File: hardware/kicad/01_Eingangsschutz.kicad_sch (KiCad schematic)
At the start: 4 parts, among them K101 G6S-2F DC5 - C16707, Q111 DMN2056U-7

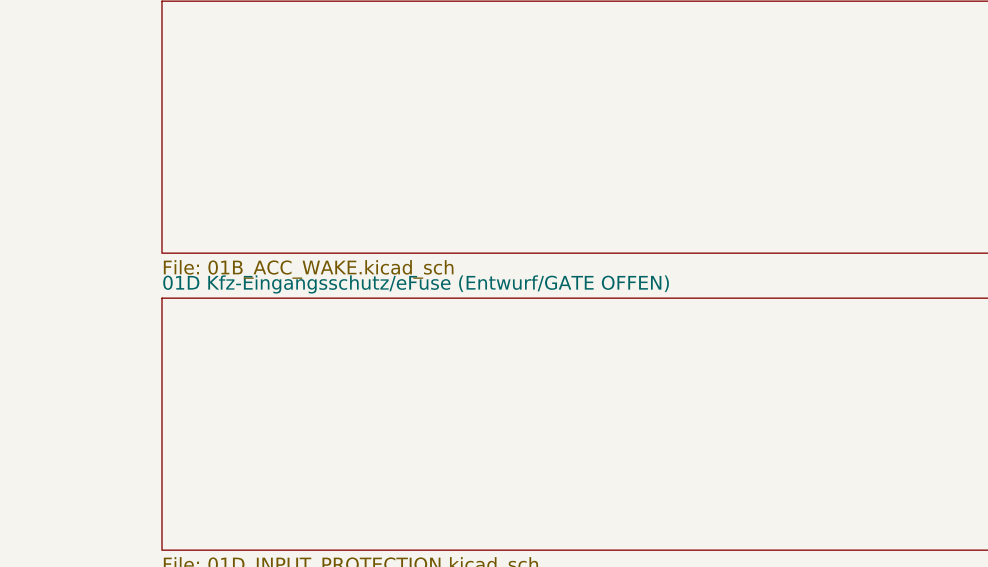
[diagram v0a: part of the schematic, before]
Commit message: hardware(kicad): mark obsolete TPS26631 sheet as retired in hierarchy
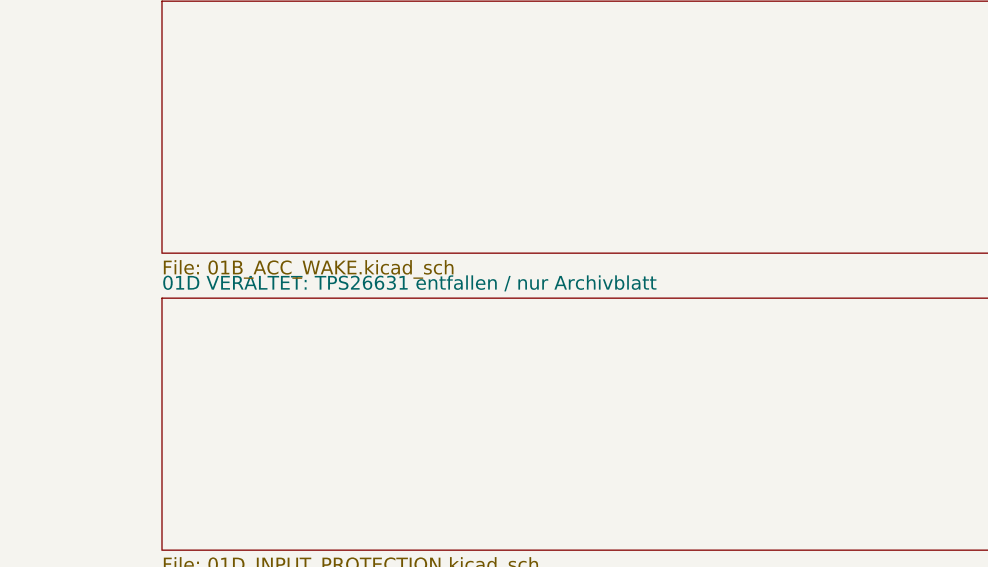
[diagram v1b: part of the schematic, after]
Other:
- sheet 01D Kfz-Eingangsschutz/eFuse (Entwurf/GATE OFFEN) renamed 01D VERALTET: TPS26631 entfallen / nur Archivblatt
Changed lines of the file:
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@@
 (sheet (at 214 290) (size 175 28) (exclude_from_sim no) (in_bom yes) (on_board yes) (dnp no)
  (stroke (width 0) (type solid)) (fill (color 0 0 0 0))
- (property "Sheetname" "01D Kfz-Eingangsschutz/eFuse (Entwurf/GATE OFFEN)" (at 214 289.24 0) (effects (font (size 1.524 1.524)) (justify left bottom)))
+ (property "Sheetname" "01D VERALTET: TPS26631 entfallen / nur Archivblatt" (at 214 289.24 0) (effects (font (size 1.524 1.524)) (justify left bottom)))
  (property "Sheetfile" "01D_INPUT_PROTECTION.kicad_sch" (at 214 318.76 0) (effects (font (size 1.524 1.524)) (justify left top)))
  (instances (project "TripTracer_V1" (path "/a26d9b0c-7f10-4e5a-a65f-000000000064/a26d9b0c-7f10-4e5a-a65f-000000000065" (page "2.4"))))

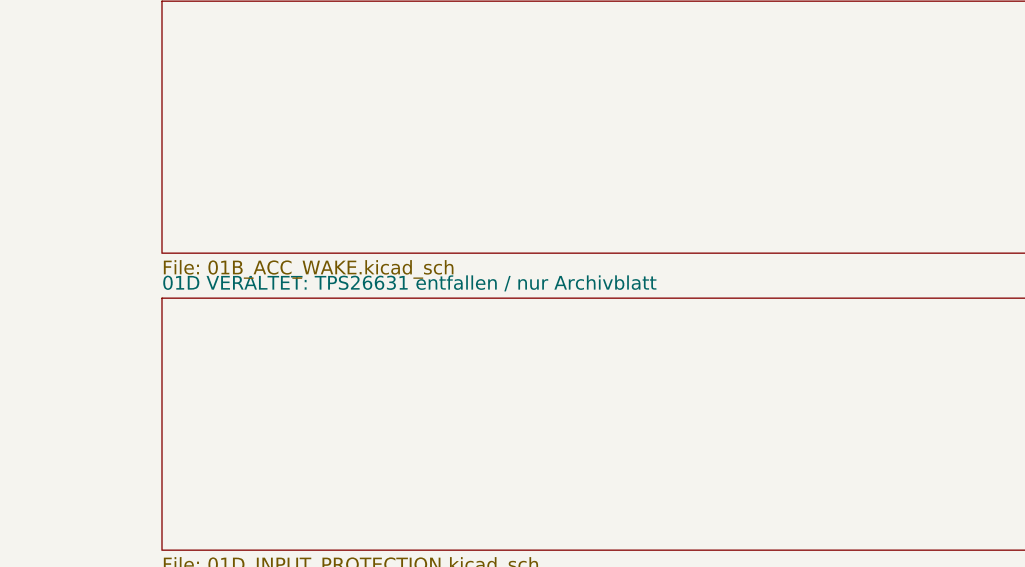
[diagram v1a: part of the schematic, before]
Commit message: hardware(kicad): identify active LM74930 core sheet in hierarchy
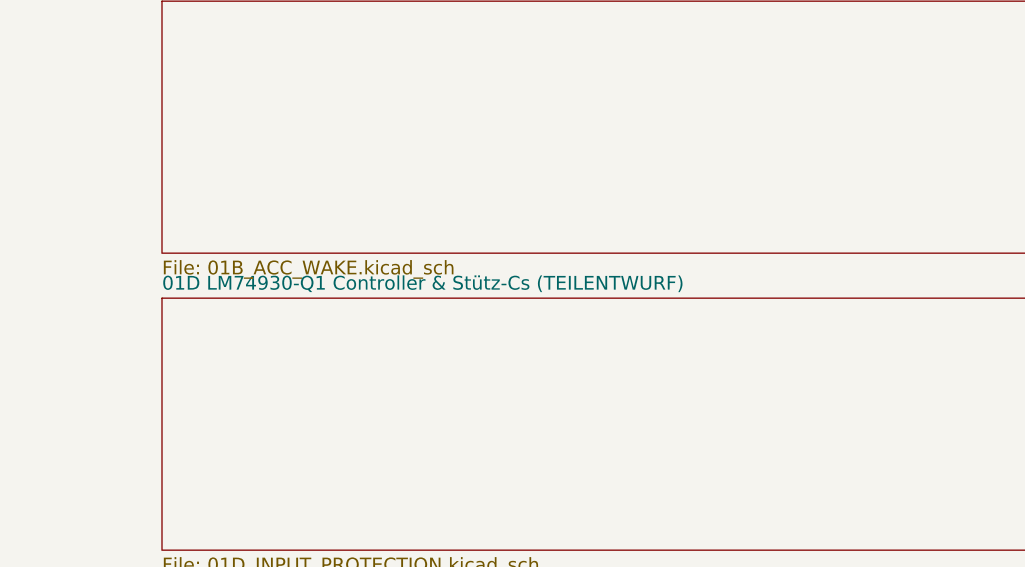
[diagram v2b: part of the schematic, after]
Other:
- sheet 01D VERALTET: TPS26631 entfallen / nur Archivblatt renamed 01D LM74930-Q1 Controller & Stütz-Cs (TEILENTWURF)
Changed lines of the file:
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@@
 (sheet (at 214 290) (size 175 28) (exclude_from_sim no) (in_bom yes) (on_board yes) (dnp no)
  (stroke (width 0) (type solid)) (fill (color 0 0 0 0))
- (property "Sheetname" "01D VERALTET: TPS26631 entfallen / nur Archivblatt" (at 214 289.24 0) (effects (font (size 1.524 1.524)) (justify left bottom)))
+ (property "Sheetname" "01D LM74930-Q1 Controller & Stütz-Cs (TEILENTWURF)" (at 214 289.24 0) (effects (font (size 1.524 1.524)) (justify left bottom)))
  (property "Sheetfile" "01D_INPUT_PROTECTION.kicad_sch" (at 214 318.76 0) (effects (font (size 1.524 1.524)) (justify left top)))
  (instances (project "TripTracer_V1" (path "/a26d9b0c-7f10-4e5a-a65f-000000000064/a26d9b0c-7f10-4e5a-a65f-000000000065" (page "2.4"))))
